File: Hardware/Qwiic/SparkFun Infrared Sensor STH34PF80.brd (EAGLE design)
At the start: 25.4 x 25.4 mm, 26 parts, among them J1 Vertical Qwiic Connector, J2 Vertical Qwiic Connector

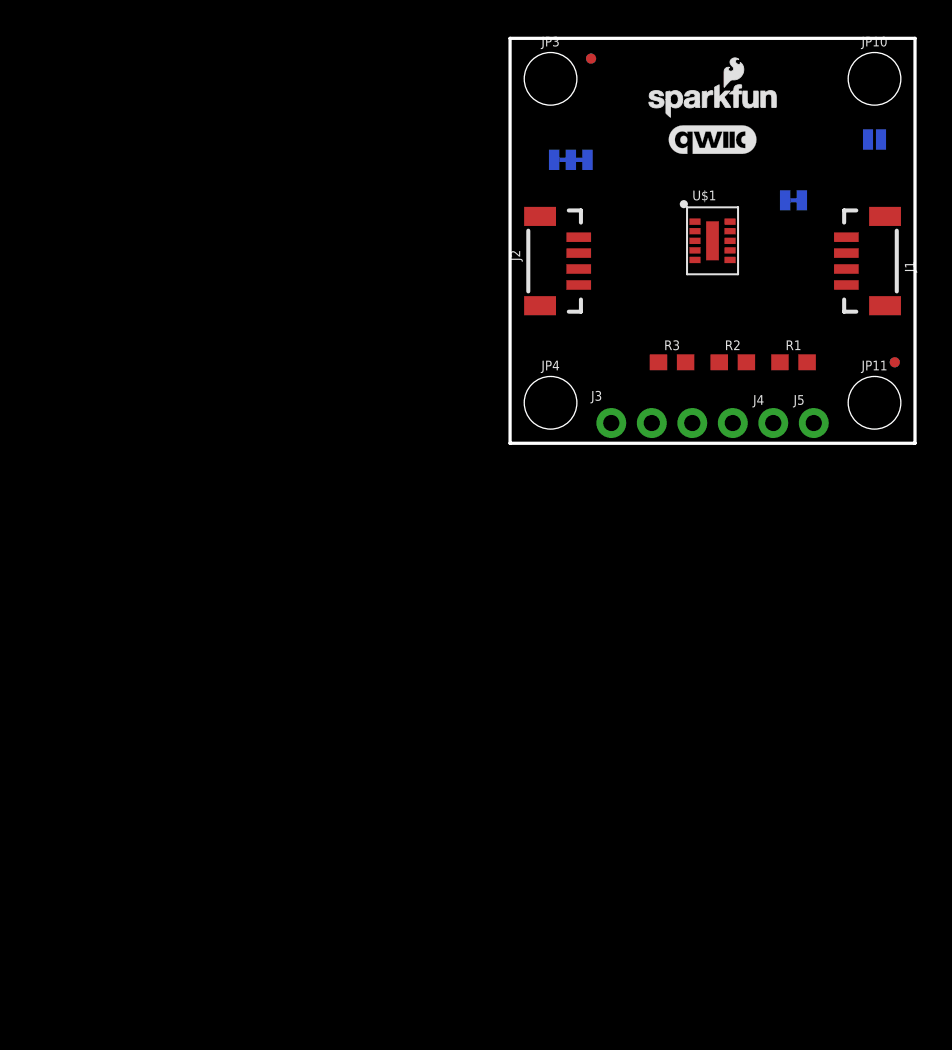
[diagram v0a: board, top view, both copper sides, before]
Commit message: Continued design
Adjusted symbol and footprint to reflect the I2C AND SPI interfaces. Uploading to change name in GitHub for official product name
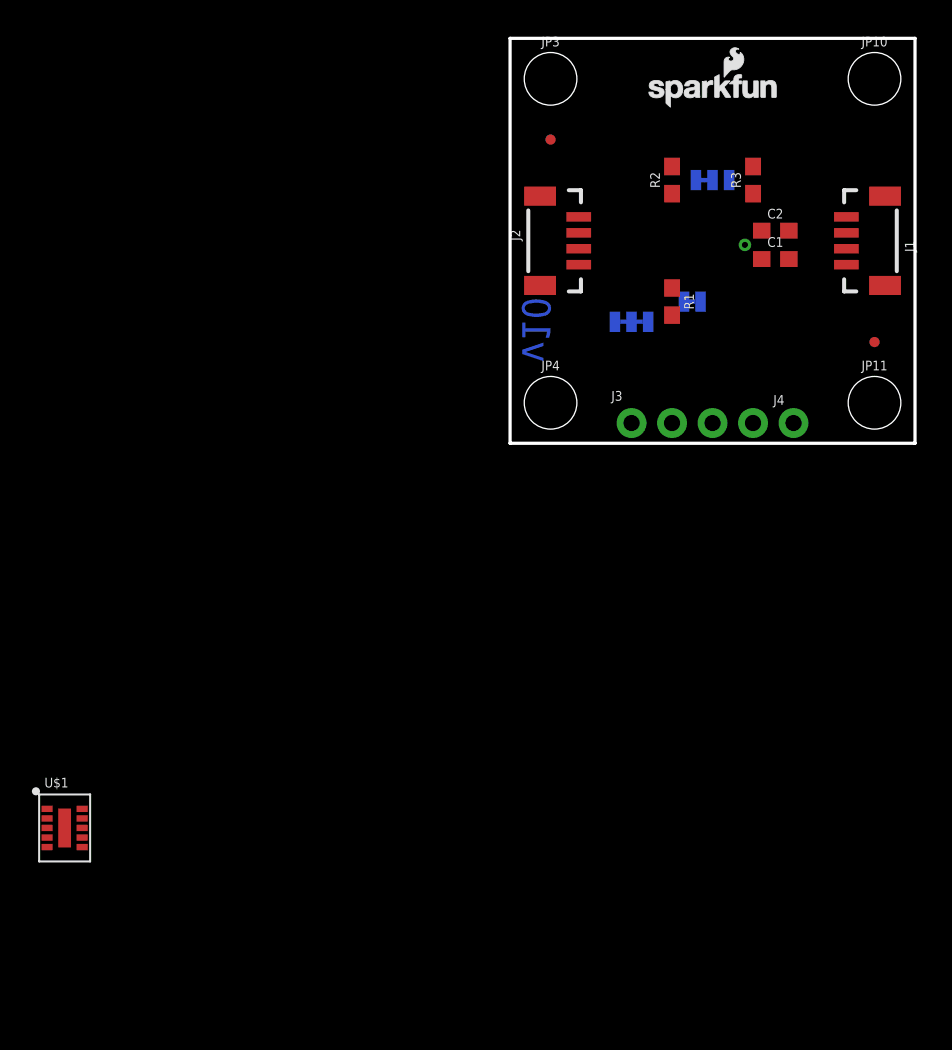
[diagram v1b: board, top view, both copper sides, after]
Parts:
- removed J5: (no value), SparkFun-Connectors:1X01_NO_SILK
- added C1: 0.1uF, SparkFun-Capacitors:0603
- added C2: 1.0uF, SparkFun-Capacitors:0603
- CS: value JUMPER-SMT_2_NO_SILK -> JUMPER-SMT_3_1-NC_TRACE_SILK; device SparkFun-Jumpers:SMT-JUMPER_2_NO_SILK -> SparkFun-Jumpers:SMT-JUMPER_3_1-NC_TRACE_SILK
- moved LOGO5 142.4 mm to (40.6, 50.8)
- moved U$1 54.8 mm to (-27.9, -24.1)
- moved LOGO3 13.5 mm to (21.6, 8.89), flipped to the bottom
- moved R3 12.5 mm to (15.2, 16.5), turned to 90 degrees
- moved R2 12.0 mm to (10.2, 16.5), turned to 90 degrees
- moved I2C 10.9 mm to (7.62, 7.62)
- moved CS 10.5 mm to (12.7, 16.5)
- moved JP9 8.98 mm to (11.4, 8.89), turned to 180 degrees
- moved R1 8.52 mm to (10.2, 8.89), turned to 270 degrees
- moved JP2 5.68 mm to (2.54, 19.1)
- moved JP5 5.68 mm to (2.54, 19.1)
- moved JP1 1.80 mm to (22.9, 6.35)
- moved JP6 1.80 mm to (22.9, 6.35)
- moved J3 1.27 mm to (7.62, 1.27)
- moved J1 1.27 mm to (20.3, 12.7)
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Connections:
- new net SCL/SCK: U$1.1
- new net SDA/SDIO: U$1.4
- net 3.3V: now also C1.1, C2.1, CS.3
- net GND: now also C1.2, C2.2, CS.1; no longer CS.2
- net INT: now also R3.1; no longer U$1.10
- net N$3: now also CS.2; no longer CS.1, U$1.3
- net N$4: now also JP9.1, R3.2; no longer J5.1
- net SCL: no longer U$1.1
- net SDA: no longer U$1.4
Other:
- board text added: "v10"

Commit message: Updates to Mini - uploading to change repo name
Continued mini board design
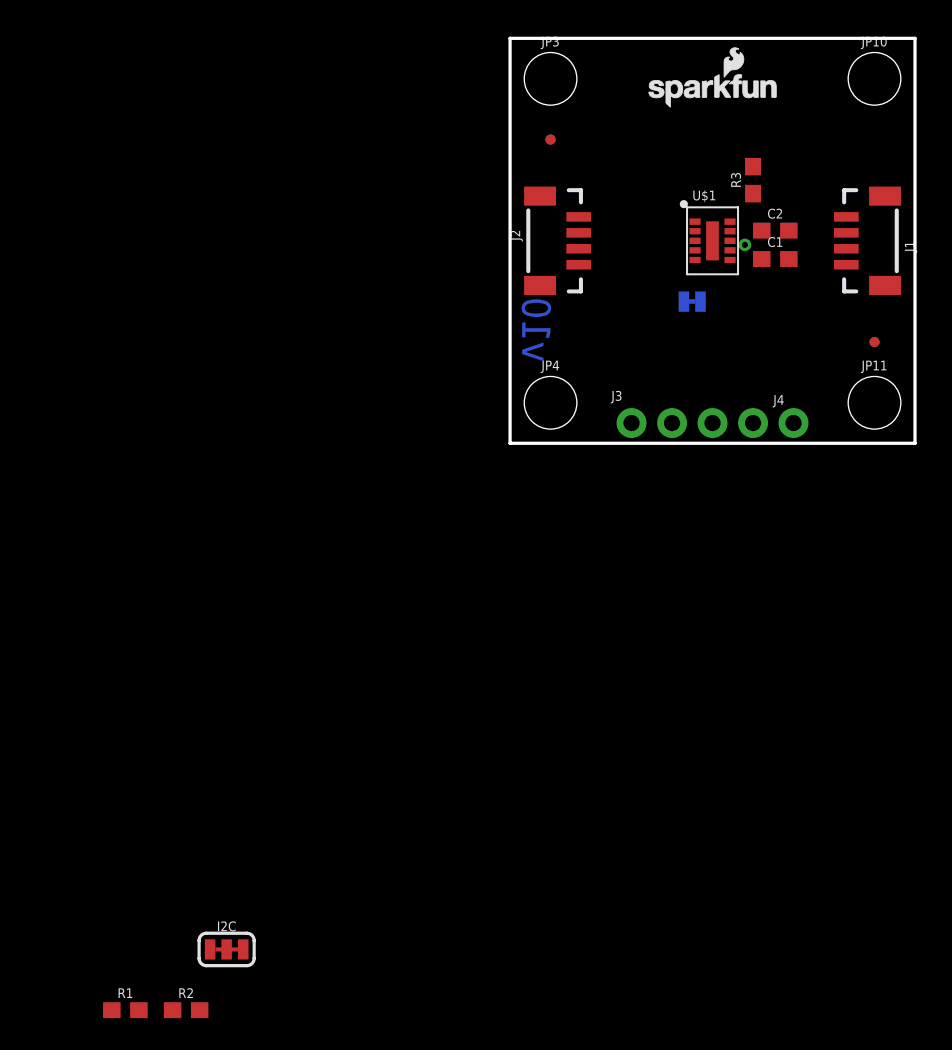
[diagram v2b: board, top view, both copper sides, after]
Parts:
- removed CS: JUMPER-SMT_3_1-NC_TRACE_SILK, SparkFun-Jumpers:SMT-JUMPER_3_1-NC_TRACE_SILK
- moved R2 60.3 mm to (-20.3, -35.6), turned to 0 degrees
- moved R1 56.1 mm to (-24.1, -35.6), turned to 0 degrees
- moved U$1 54.8 mm to (12.7, 12.7)
- moved I2C 46.9 mm to (-17.8, -31.8), flipped to the top
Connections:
- removed net N$3: CS.2
- net 3.3V: no longer CS.3
- net GND: no longer CS.1
